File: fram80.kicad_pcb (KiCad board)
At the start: 2 copper layers, 51.8 x 17.3 mm, 12 parts, among them J1 UPPER, J2 LOWER, U1 FM1808B-SG, U3 74LS00

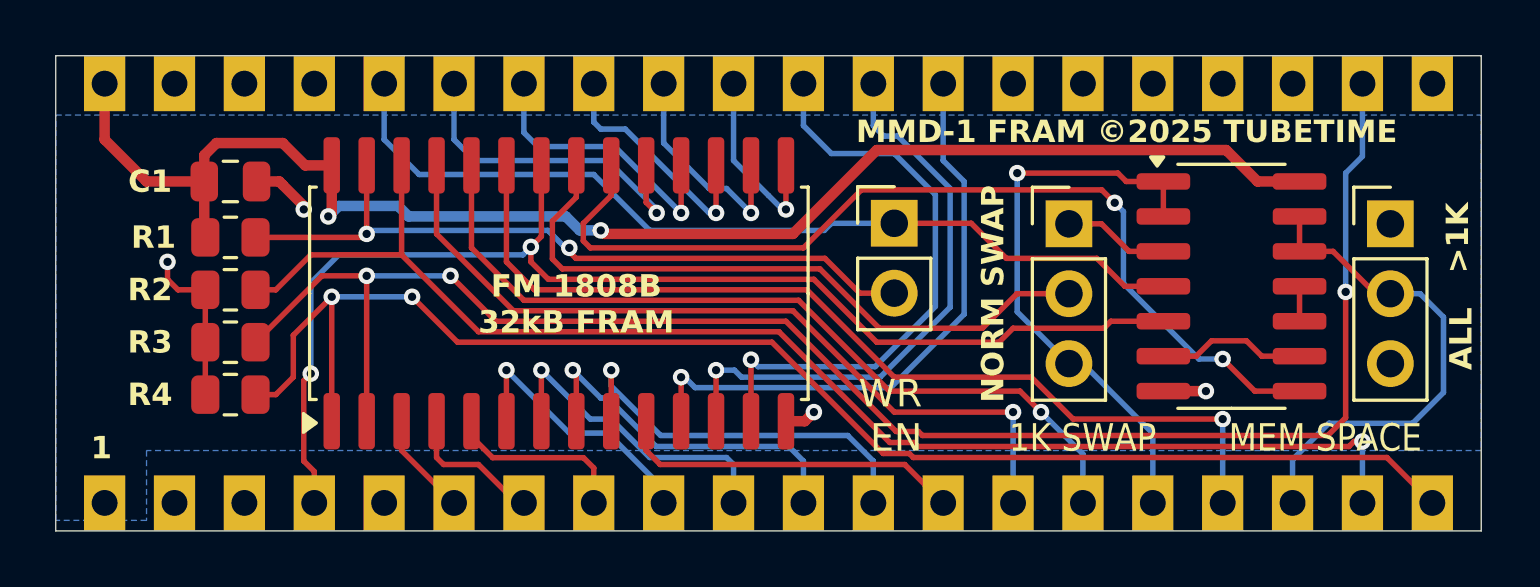
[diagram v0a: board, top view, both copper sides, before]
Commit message: Support upper 32K
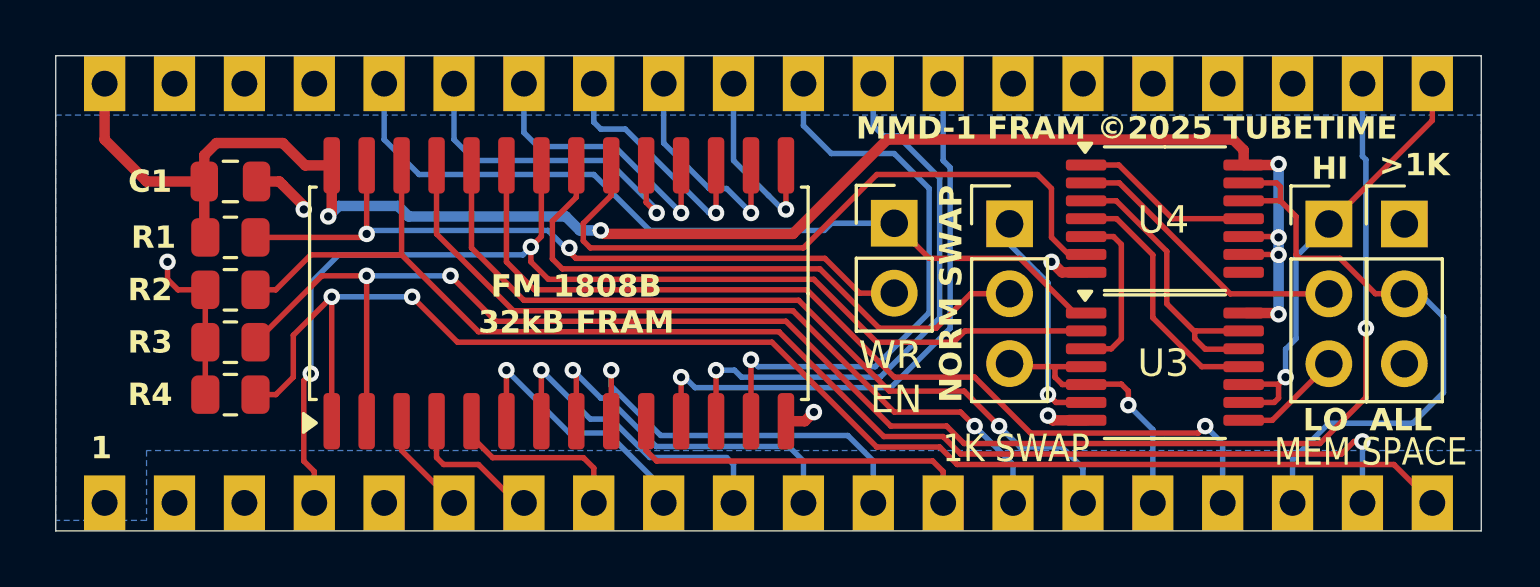
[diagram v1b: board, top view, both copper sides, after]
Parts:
- added JP4: UPPER, Connector_PinHeader_2.54mm:PinHeader_1x03_P2.54mm_Vertical, F.Cu at (171.5, 68.6)
- added U4: 74HCT00, Package_SO:TSSOP-14_4.4x5mm_P0.65mm, F.Cu at (165.5, 68.4)
- U3: value 74LS00 -> 74HCT00; footprint Package_SO:SO-14_3.9x8.65mm_P1.27mm -> Package_SO:TSSOP-14_4.4x5mm_P0.65mm
- moved U3 3.79 mm to (165.5, 73.8)
- moved JP2 2.16 mm to (159.9, 68.6)
- moved JP1 0.51 mm to (174.2, 68.6)
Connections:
- J1 pad 20: unconnected-(J1-Pin_20-Pad20) -> /A15
- U3 pad 1: /A10 -> /~{MEMW}
- U3 pad 10: Net-(U3-Pad10) -> /A15
- U3 pad 11: Net-(U3-Pad10) -> Net-(U3-Pad11)
- U3 pad 12: /~{SEL0} -> Net-(U3-Pad12)
- U3 pad 13: /~{SEL0} -> Net-(U3-Pad12)
- U3 pad 2: /A10 -> /~{MEMR}
- U3 pad 3: /~{A10} -> Net-(U3-Pad3)
- U3 pad 4: /~{MEMW} -> /A10
- U3 pad 5: /~{MEMR} -> /A10
- U3 pad 6: Net-(U3-Pad6) -> /~{A10}
- U3 pad 8: /~{CS} -> /~{A15}
- U3 pad 9: Net-(U3-Pad6) -> /A15
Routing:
- net /A15: track 0.00 -> 16.4 mm, vias 0 -> 1
- net Net-(U3-Pad12): track 0.00 -> 11.0 mm
- net Net-(JP4-C): track 0.00 -> 10.5 mm
- net /A10: track 20.5 -> 10.5 mm
- net /~{CS}: track 34.7 -> 24.9 mm, vias 2 -> 0
- net Net-(U3-Pad11): track 0.00 -> 9.29 mm
- net +5V: track 54.0 -> 62.8 mm, vias 2 -> 6
- net Net-(U4-Pad1): track 0.00 -> 6.53 mm
- net Net-(U3-Pad3): track 0.00 -> 6.26 mm
- net Net-(U3-Pad6): track 5.41 -> 0.00 mm
- net /~{A10}: track 3.34 -> 8.29 mm, vias 0 -> 1
- net /~{SEL0}: track 18.3 -> 22.6 mm
- net /~{A15}: track 0.00 -> 3.95 mm
- net /~{MEMR}: track 45.0 -> 42.0 mm
- net /A10B: track 24.6 -> 21.9 mm
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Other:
- board text added: "A15"
- board text added: "HI"
- board text added: "LO"
- board text removed: "nc"
